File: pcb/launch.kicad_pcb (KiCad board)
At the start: 4 copper layers, 299 x 127 mm, 370 parts, among them J0 12401598E4#2A, J1 DNP, J2 1003-002-01100, J3 1003-002-01100, J4 12401598E4#2A, J5 12401598E4#2A, U0 USBLC6-2SC6, U1 ATmega32U4-MU, U10 AP22811AW5-7, U11 PTN5110DHQ, U12 PTN5110THQ, U13 PTN5110THQ, U14 SN74LVC1G08DCKR, U15 CBTL02043ABQ,115, U16 AP22811AW5-7‎, U17 TLV62585PDRLR, U18 LP5907MFX-3.3, U19 SN74LVC1G08DCKR, U2 USB7206, U20 AP22811AW5-7, U21 USBLC6-2SC6, U22 AP22811AW5-7, U23 AP22811AW5-7, U3 CBTL02043ABQ,115, U4 TLV62585PDRLR, U5 USBLC6-2SC6, U6 CBTL02043ABQ,115, U7 USBLC6-2SC6, U8 USBLC6-2SC6, U9 AP22811AW5-7, X1 ECS-3225MV-250-BN-TR, Y0 ECS-160-18-23G-JGN-TR

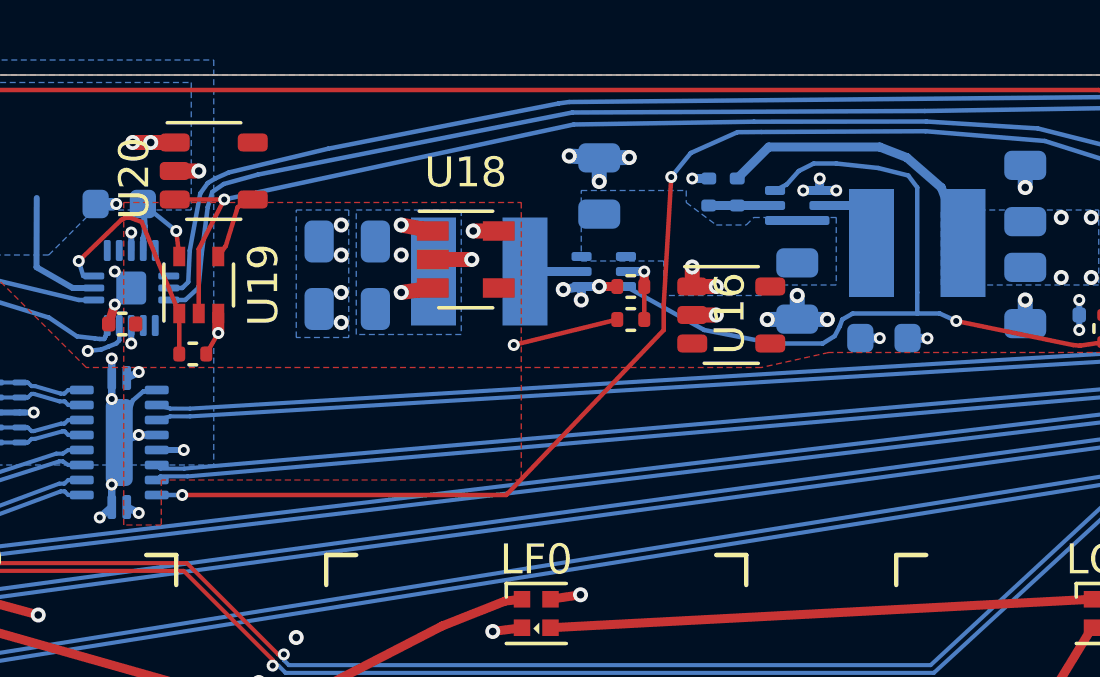
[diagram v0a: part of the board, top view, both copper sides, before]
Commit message: Switch to AP3441LSHE-7B in PCB
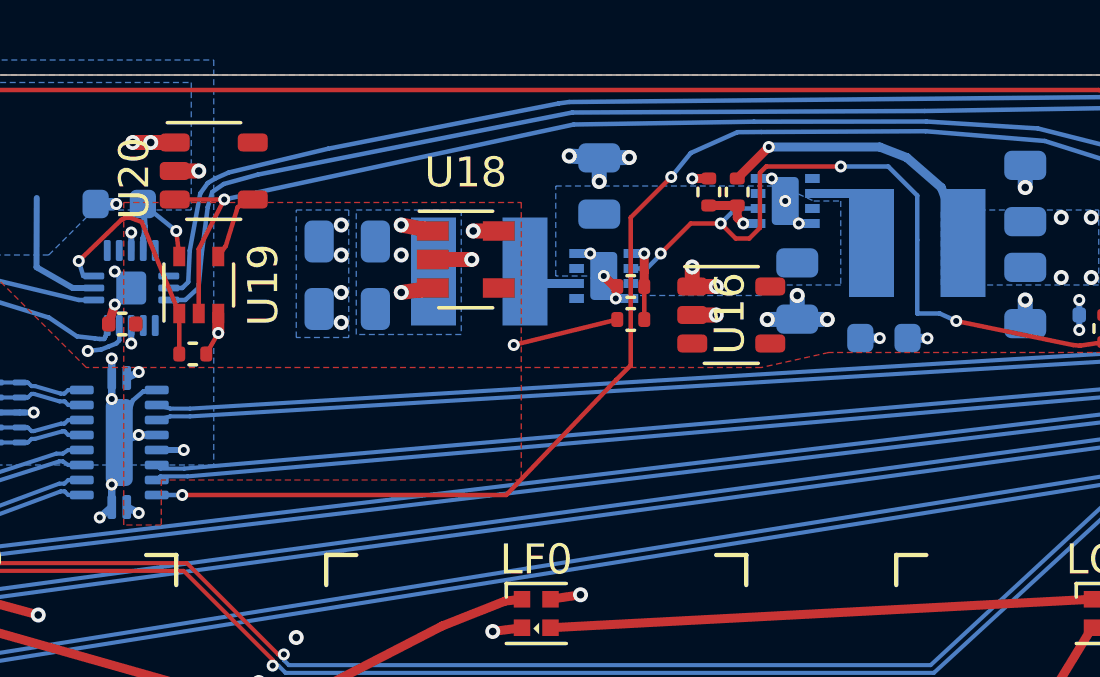
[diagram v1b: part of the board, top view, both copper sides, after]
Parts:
- C32, C34, C35, C48, C49, C50: value 10 uF -> 22 uF
- R14, R15: moved to F.Cu
- U17, U4: value TLV62585PDRLR -> AP3441LSHE-7B; footprint launch:SOT-563 -> launch:W-DFN2020-8_Type_C
- moved U17 0.43 mm to (113.3, -8.80), turned to 0 degrees
- moved U4 0.15 mm to (107.2, -6.30), turned to 180 degrees
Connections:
- U17 pad 1: GND -> /power/FB1V1
- U17 pad 2: /power/SW1V1 -> /USB/~RESET
- U17 pad 4: VCC -> GND
- U17 pad 5: /power/FB1V1 -> (no net)
- U17 pad 6: /USB/~RESET -> /power/SW1V1
- U4 pad 1: GND -> /power/FB3V6
- U4 pad 2: /power/SW3V6 -> /USB/~RESET
- U4 pad 4: VCC -> GND
- U4 pad 5: /power/FB3V6 -> (no net)
- U4 pad 6: /USB/~RESET -> /power/SW3V6
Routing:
- net GND: track 247.6 -> 250.0 mm
- net /USB/~RESET: track 44.2 -> 42.4 mm, vias 2 -> 5
- net VCC: track 2.93 -> 1.45 mm
- net /power/FB1V1: track 2.21 -> 2.13 mm, vias 0 -> 1
- net +1V1: vias 13 -> 14

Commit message: Update PCB to revision 1.2
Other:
- board text added: "Launch Rev 1.2 Board must be RoHS compliant Fabricate to IPC-A-600 Class II Material: Shengyi S1000-2 Inner copper 1 or 1/2 oz Outer copper, min 33.4 um finished Black LPI solder mask over bare copper Vendor may remove solder mask from via holes, maximum of drill size + 3 mil Finish: OSP Silkscreen: white non conductive 100% electrical test required Remove all unused pads from inner layers All la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"
- board text added: "launch_1.2"
- board text removed: "Launch Rev 1.1 Board must be RoHS compliant Fabricate to IPC-A-600 Class II Material: Shengyi S1000-2 Inner copper 1 or 1/2 oz Outer copper, min 33.4 um finished Black LPI solder mask over bare copper Vendor may remove solder mask from via holes, maximum of drill size + 3 mil Finish: OSP Silkscreen: white non conductive 100% electrical test required Remove all unused pads from inner layers All la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"
- board text removed: "launch_1.1"

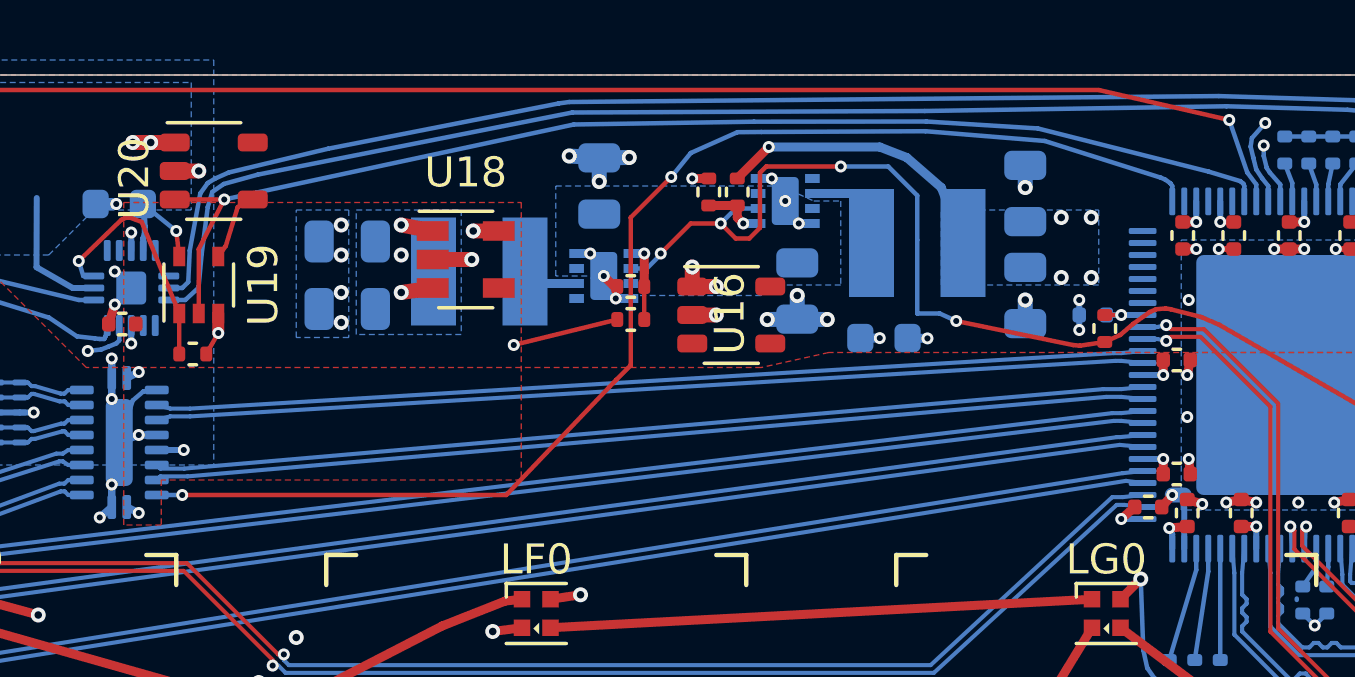
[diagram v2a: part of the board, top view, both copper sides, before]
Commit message: Add 22pF capacitors to AP3441-L as recommended
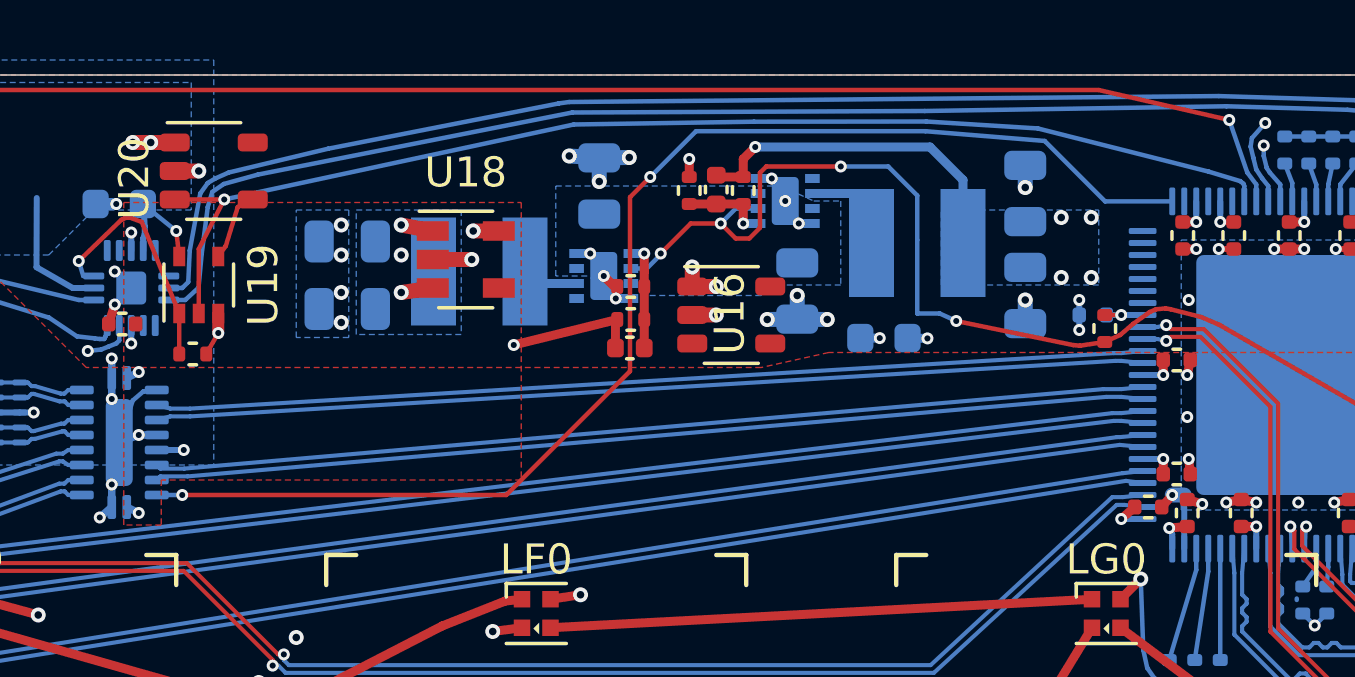
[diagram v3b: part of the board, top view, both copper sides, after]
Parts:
- added C68: 22 pF, Capacitor_SMD:C_0402_1005Metric, F.Cu at (111.0, -9.18)
- added C69: 22 pF, Capacitor_SMD:C_0402_1005Metric, F.Cu at (108.1, -3.90)
- moved R15 0.65 mm to (110.1, -9.15)
- moved R14 0.21 mm to (111.9, -9.15)
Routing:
- net +1V1: track 20.4 -> 22.3 mm
- net +3V6: track 147.9 -> 148.9 mm
- net /power/FB3V6: track 2.64 -> 3.59 mm
- net /power/FB1V1: track 2.13 -> 2.95 mm
- net /USB/CL_SEL: track 42.5 -> 43.1 mm
